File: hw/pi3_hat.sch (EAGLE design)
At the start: 113 parts, among them J1 XT30P, J2 XT30P, U1 AP64351SO8EP, U10 CAT24C32SOIC8, U11 STM32G474CEU6, U12 TCAN334GSOT23, U13 TCAN334GSOT23, U2 DMMT5401, U3 DMG2305UX, U4 STM32G474CEU6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

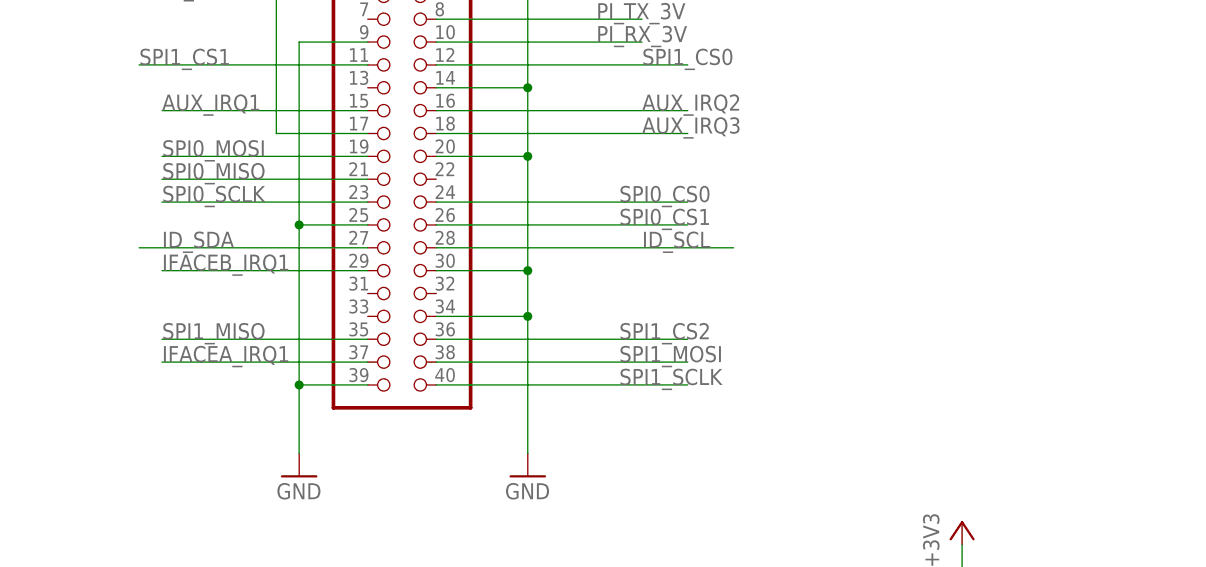
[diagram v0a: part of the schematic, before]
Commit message: Stick two rpi pins on a header and fix silks
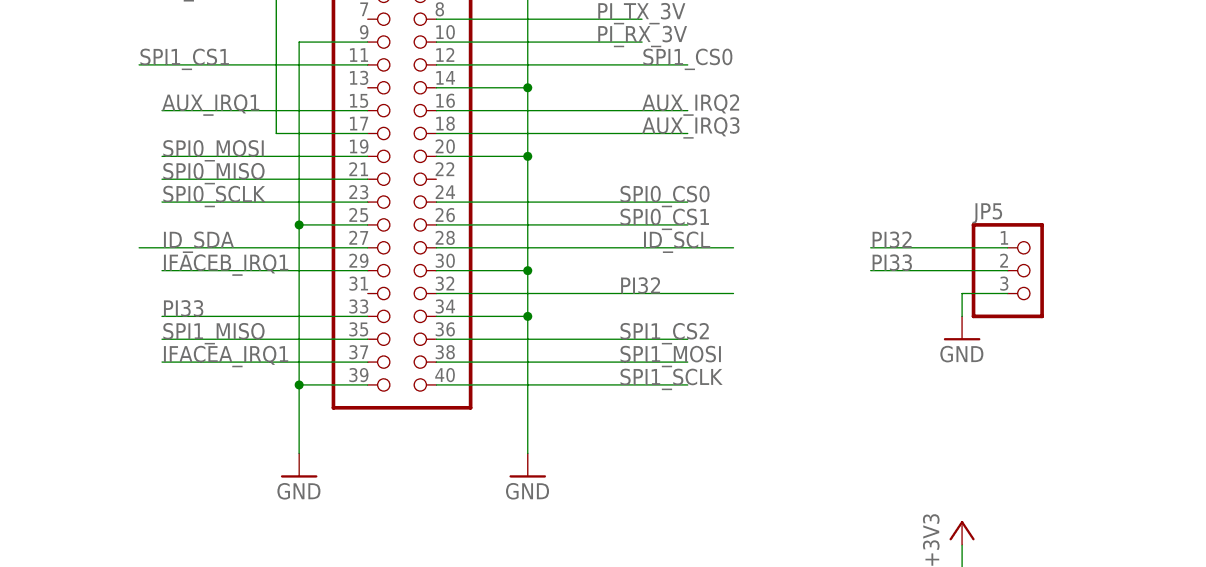
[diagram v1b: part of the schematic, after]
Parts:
- added JP5: (no value), pinhead:PINHD-1X3
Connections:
- new net PI32: J4.32, JP5.1
- new net PI33: J4.33, JP5.2
- net GND: now also JP5.3
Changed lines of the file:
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@@
 </part>
 <part name="GND59" library="supply1" deviceset="GND" device=""/>
+<part name="JP5" library="pinhead" library_urn="urn:adsk.eagle:library:325" deviceset="PINHD-1X3" device="" package3d_urn="urn:adsk.eagle:package:22458/2">
+<attribute name="MF" value="MacroFab"/>
+<attribute name="MPN" value="MF-CON-2.54mm-01x03"/>
+<attribute name="POPULATE" value="1"/>
+</part>
+<part name="GND60" library="supply1" deviceset="GND" device=""/>
 </parts>
 <sheets>
@@
 <attribute name="VALUE" x="403.86" y="213.36" size="1.778" layer="96"/>
 </instance>
+<instance part="JP5" gate="A" x="127" y="86.36" smashed="yes">
+<attribute name="NAME" x="120.65" y="92.075" size="1.778" layer="95"/>
+<attribute name="VALUE" x="120.65" y="78.74" size="1.778" layer="96"/>
+<attribute name="MF" x="127" y="86.36" size="1.778" layer="96" display="off"/>
+<attribute name="MPN" x="127" y="86.36" size="1.778" layer="96" display="off"/>
+<attribute name="POPULATE" x="127" y="86.36" size="1.778" layer="96" display="off"/>
+</instance>
+<instance part="GND60" gate="1" x="119.38" y="78.74" smashed="yes">
+<attribute name="VALUE" x="116.84" y="76.2" size="1.778" layer="96"/>
+</instance>
 </instances>
 <busses>
@@
 <pinref part="GND59" gate="1" pin="GND"/>
 <wire x1="406.4" y1="220.98" x2="406.4" y2="218.44" width="0.1524" layer="91"/>
+</segment>
+<segment>
+<pinref part="JP5" gate="A" pin="3"/>
+<wire x1="124.46" y1="83.82" x2="119.38" y2="83.82" width="0.1524" layer="91"/>
+<pinref part="GND60" gate="1" pin="GND"/>
+<wire x1="119.38" y1="83.82" x2="119.38" y2="81.28" width="0.1524" layer="91"/>
 </segment>
 </net>
@@
 </segment>
 </net>
+<net name="PI33" class="0">
+<segment>
+<pinref part="JP5" gate="A" pin="2"/>
+<wire x1="124.46" y1="86.36" x2="109.22" y2="86.36" width="0.1524" layer="91"/>
+<label x="109.22" y="86.36" size="1.778" layer="95"/>
+</segment>
+<segment>
+<pinref part="J4" gate="A" pin="33"/>
+<wire x1="53.34" y1="81.28" x2="30.48" y2="81.28" width="0.1524" layer="91"/>
+<label x="30.48" y="81.28" size="1.778" layer="95"/>
+</segment>
+</net>
+<net name="PI32" class="0">
+<segment>
+<pinref part="JP5" gate="A" pin="1"/>
+<wire x1="124.46" y1="88.9" x2="109.22" y2="88.9" width="0.1524" layer="91"/>
+<label x="109.22" y="88.9" size="1.778" layer="95"/>
+</segment>
+<segment>
+<pinref part="J4" gate="A" pin="32"/>
+<wire x1="60.96" y1="83.82" x2="93.98" y2="83.82" width="0.1524" layer="91"/>
+<label x="81.28" y="83.82" size="1.778" layer="95"/>
+</segment>
+</net>

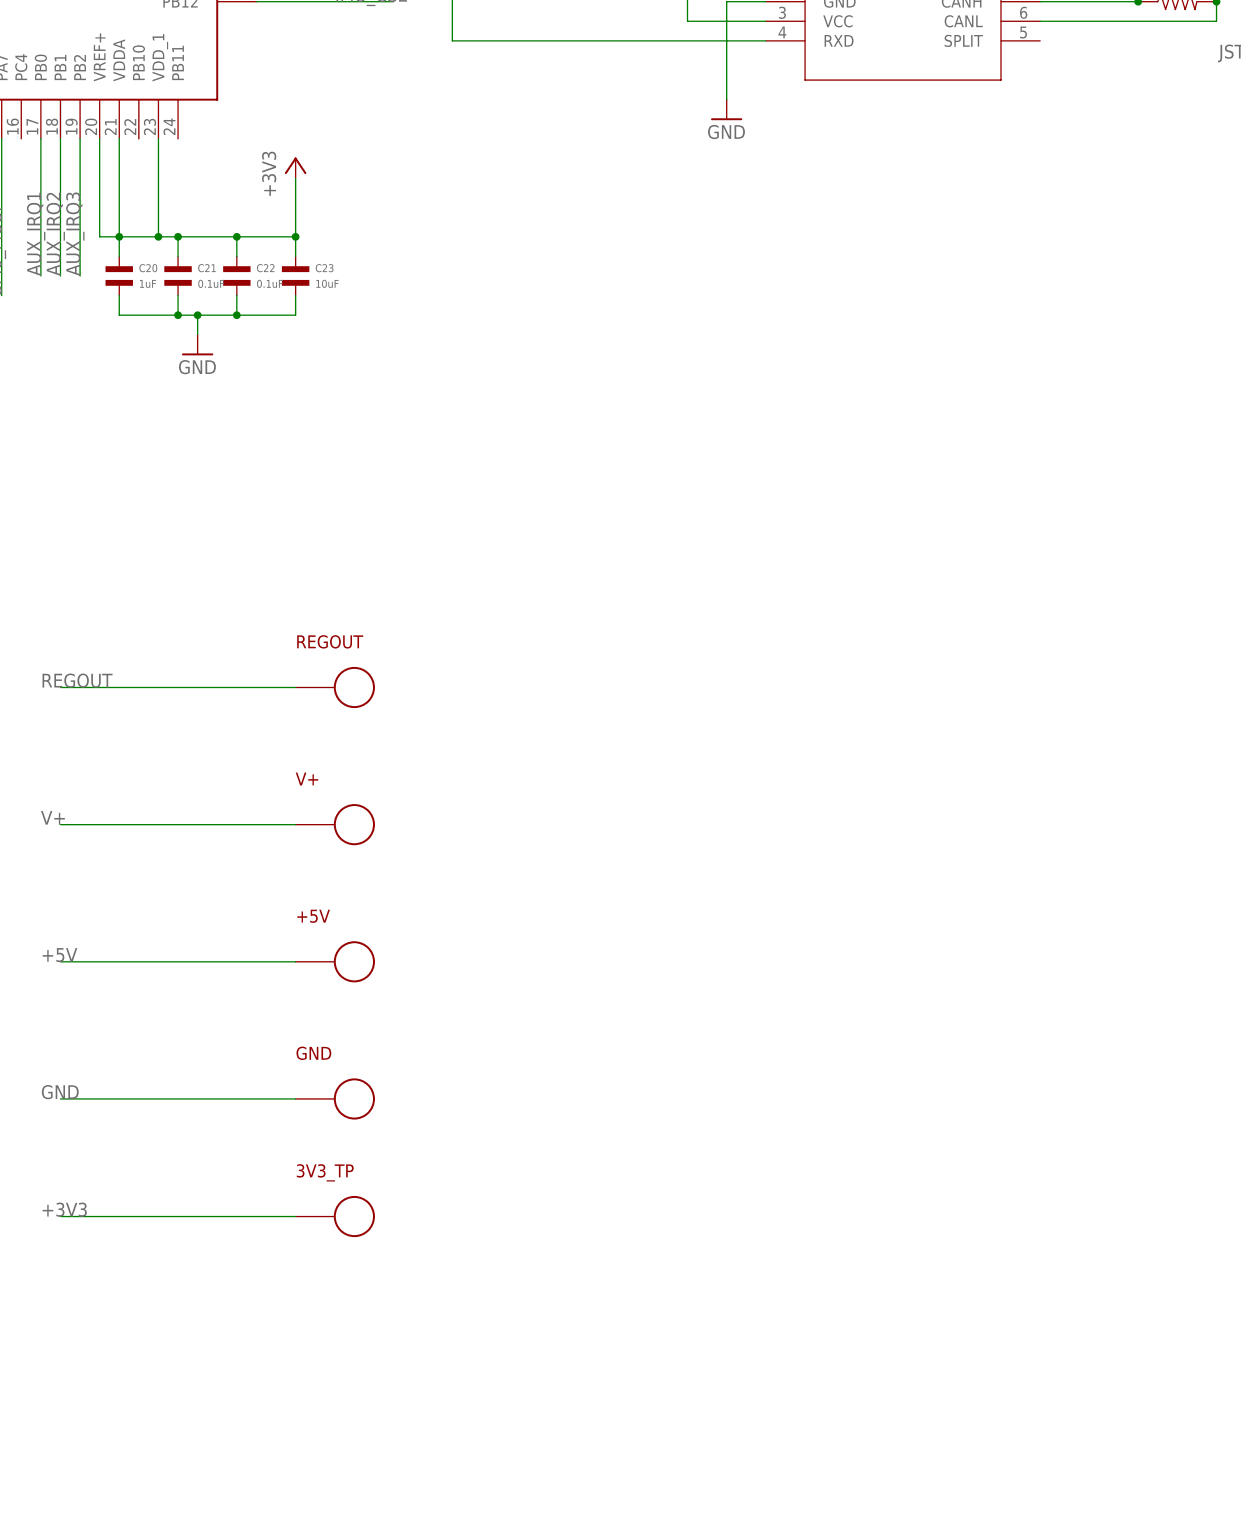
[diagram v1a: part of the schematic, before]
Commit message: Add microphone to aux processor
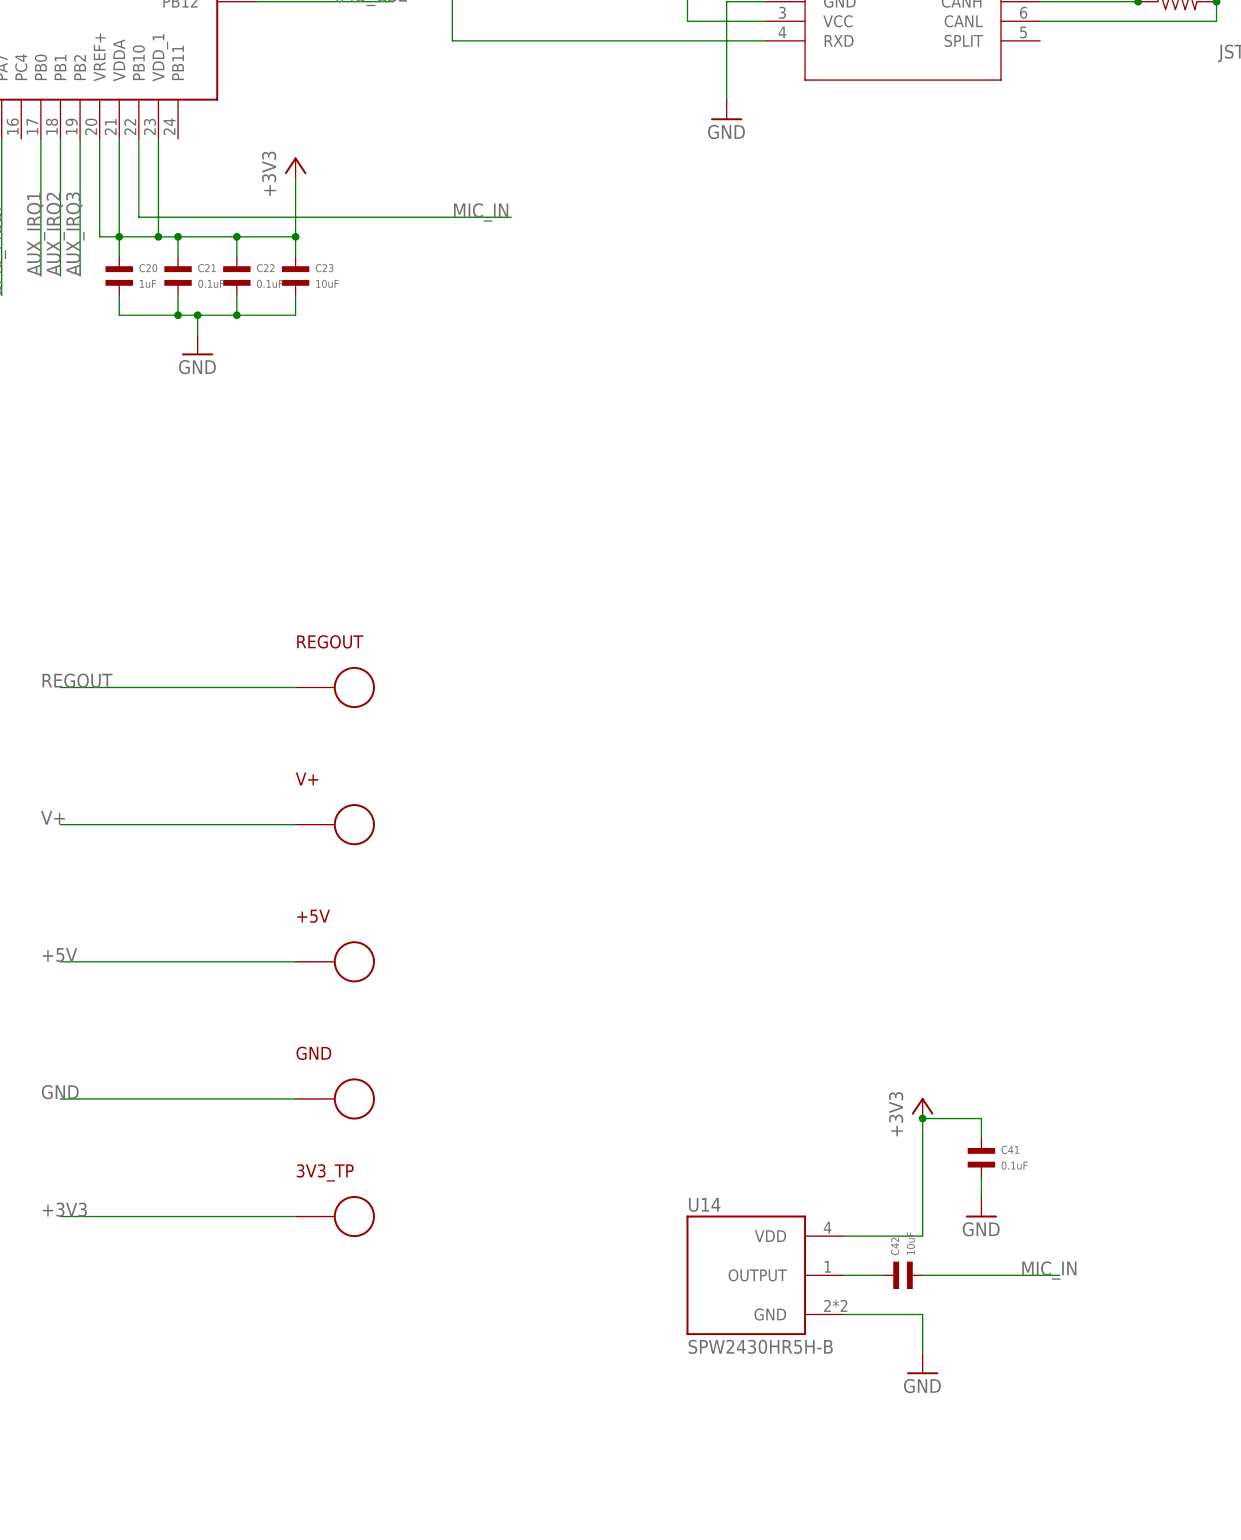
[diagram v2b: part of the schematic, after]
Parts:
- added C41: 0.1uF, mfpassives:CAPACITOR_NP_0402
- added C42: 10uF, mfpassives:CAPACITOR_NP_1206
- added U14: SPW2430HR5H-B, SPW2430HR5H-B:SPW2430HR5H-B
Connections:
- new net MIC_IN: C42.P$2, U7.PB10
- new net N$59: C42.P$1, U14.OUTPUT
- net +3V3: now also C41.P$1, U14.VDD
- net GND: now also C41.P$2, U14.GND
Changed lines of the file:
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@@
 </part>
 <part name="GND60" library="supply1" deviceset="GND" device=""/>
+<part name="U14" library="SPW2430HR5H-B" deviceset="SPW2430HR5H-B" device="">
+<attribute name="MPN" value="SPW2430HR5H-B"/>
+<attribute name="POPULATE" value="1"/>
+</part>
+<part name="GND61" library="supply1" deviceset="GND" device=""/>
+<part name="+3V33" library="supply1" deviceset="+3V3" device=""/>
+<part name="C41" library="mfpassives" deviceset="CAPACITOR_NP" device="_0402" value="0.1uF">
+<attribute name="HOUSEPART" value="YES"/>
+<attribute name="MPN" value="MF-CAP-0402-0.1uF"/>
+</part>
+<part name="GND62" library="supply1" deviceset="GND" device=""/>
+<part name="C42" library="mfpassives" deviceset="CAPACITOR_NP" device="_1206" value="10uF">
+<attribute name="HOUSEPART" value="YES"/>
+<attribute name="MPN" value="MF-CAP-1206-10uF"/>
+</part>
 </parts>
 <sheets>
@@
 <attribute name="VALUE" x="116.84" y="76.2" size="1.778" layer="96"/>
 </instance>
+<instance part="U14" gate="G$1" x="779.78" y="58.42" smashed="yes">
+<attribute name="NAME" x="772.16" y="66.675" size="1.778" layer="95"/>
+<attribute name="VALUE" x="772.16" y="48.26" size="1.778" layer="96"/>
+<attribute name="MPN" x="779.78" y="58.42" size="1.778" layer="96" display="off"/>
+<attribute name="POPULATE" x="779.78" y="58.42" size="1.778" layer="96" display="off"/>
+</instance>
+<instance part="GND61" gate="1" x="802.64" y="45.72" smashed="yes">
+<attribute name="VALUE" x="800.1" y="43.18" size="1.778" layer="96"/>
+</instance>
+<instance part="+3V33" gate="G$1" x="802.64" y="81.28" smashed="yes">
+<attribute name="VALUE" x="800.1" y="76.2" size="1.778" layer="96" rot="R90"/>
+</instance>
+<instance part="C41" gate="G$1" x="810.26" y="73.66" smashed="yes">
+<attribute name="NAME" x="812.8" y="75.184" size="1.016" layer="95" font="vector" align="top-left"/>
+<attribute name="VALUE" x="812.8" y="72.136" size="1.016" layer="96" font="vector"/>
+</instance>
+<instance part="GND62" gate="1" x="810.26" y="66.04" smashed="yes">
+<attribute name="VALUE" x="807.72" y="63.5" size="1.778" layer="96"/>
+</instance>
+<instance part="C42" gate="G$1" x="800.1" y="58.42" smashed="yes" rot="R90">
+<attribute name="NAME" x="798.576" y="60.96" size="1.016" layer="95" font="vector" rot="R90" align="top-left"/>
+<attribute name="VALUE" x="801.624" y="60.96" size="1.016" layer="96" font="vector" rot="R90"/>
+</instance>
 </instances>
 <busses>
@@
 <pinref part="GND60" gate="1" pin="GND"/>
 <wire x1="119.38" y1="83.82" x2="119.38" y2="81.28" width="0.1524" layer="91"/>
+</segment>
+<segment>
+<pinref part="GND62" gate="1" pin="GND"/>
+<pinref part="C41" gate="G$1" pin="P$2"/>
+<wire x1="810.26" y1="68.58" x2="810.26" y2="71.12" width="0.1524" layer="91"/>
+</segment>
+<segment>
+<pinref part="GND61" gate="1" pin="GND"/>
+<wire x1="802.64" y1="48.26" x2="802.64" y2="53.34" width="0.1524" layer="91"/>
+<pinref part="U14" gate="G$1" pin="GND"/>
+<wire x1="802.64" y1="53.34" x2="792.48" y2="53.34" width="0.1524" layer="91"/>
 </segment>
 </net>
@@
 <label x="688.34" y="66.04" size="1.778" layer="95"/>
 </segment>
+<segment>
+<pinref part="C41" gate="G$1" pin="P$1"/>
+<wire x1="810.26" y1="76.2" x2="810.26" y2="78.74" width="0.1524" layer="91"/>
+<pinref part="+3V33" gate="G$1" pin="+3V3"/>
+<wire x1="810.26" y1="78.74" x2="802.64" y2="78.74" width="0.1524" layer="91"/>
+<wire x1="802.64" y1="78.74" x2="802.64" y2="63.5" width="0.1524" layer="91"/>
+<junction x="802.64" y="78.74"/>
+<pinref part="U14" gate="G$1" pin="VDD"/>
+<wire x1="802.64" y1="63.5" x2="792.48" y2="63.5" width="0.1524" layer="91"/>
+</segment>
 </net>
 <net name="PI_TX_3V" class="0">
@@
 </segment>
 </net>
+<net name="N$59" class="0">
+<segment>
+<pinref part="U14" gate="G$1" pin="OUTPUT"/>
+<pinref part="C42" gate="G$1" pin="P$1"/>
+<wire x1="792.48" y1="58.42" x2="797.56" y2="58.42" width="0.1524" layer="91"/>
+</segment>
+</net>
+<net name="MIC_IN" class="0">
+<segment>
+<pinref part="C42" gate="G$1" pin="P$2"/>
+<wire x1="802.64" y1="58.42" x2="820.42" y2="58.42" width="0.1524" layer="91"/>
+<label x="815.34" y="58.42" size="1.778" layer="95"/>
+</segment>
+<segment>
+<pinref part="U7" gate="G$1" pin="PB10"/>
+<wire x1="701.04" y1="205.74" x2="701.04" y2="195.58" width="0.1524" layer="91"/>
+<wire x1="701.04" y1="195.58" x2="749.3" y2="195.58" width="0.1524" layer="91"/>
+<label x="741.68" y="195.58" size="1.778" layer="95"/>
+</segment>
+</net>
